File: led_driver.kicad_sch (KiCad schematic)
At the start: 19 parts, among them U1 MP2483DQ-LF-P

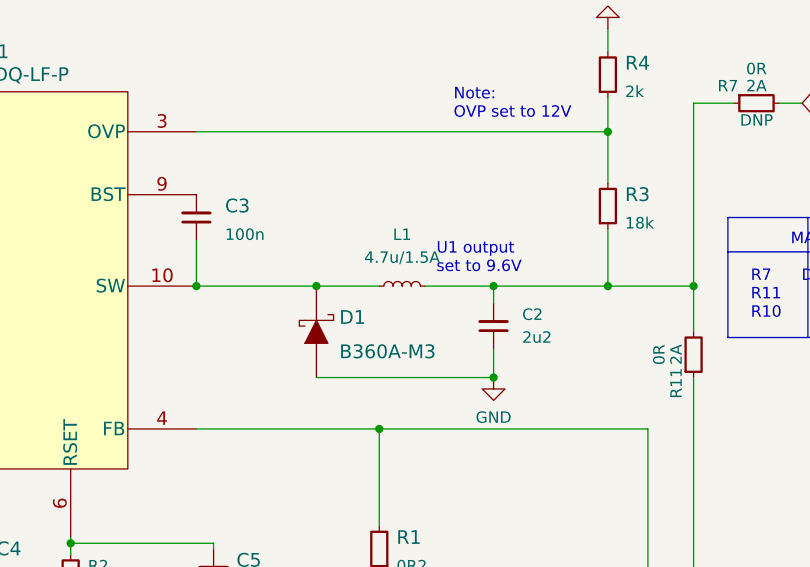
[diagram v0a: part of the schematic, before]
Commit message: Layout tweaks
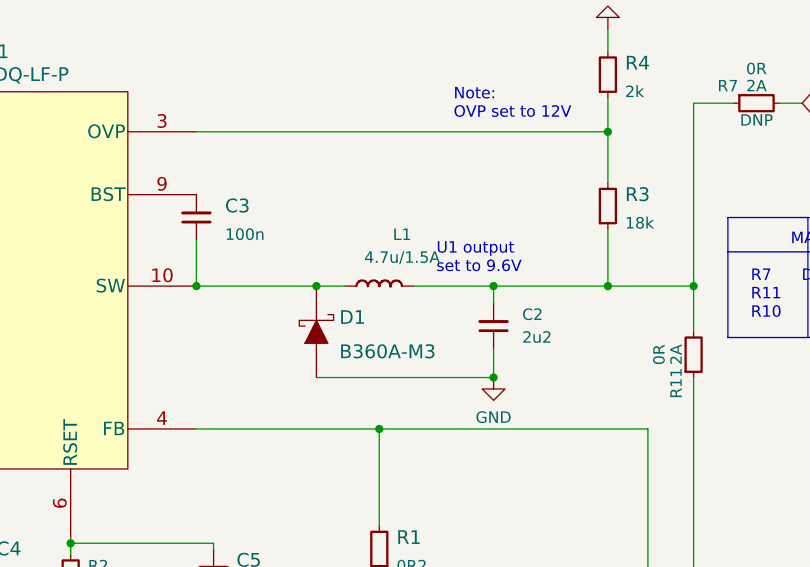
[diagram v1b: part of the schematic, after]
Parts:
- POT1: footprint antmicro-footprints:R0141-2-20k -> antmicro-footprints:Potentiometer_SRPassives_R0141-2_Horizontal
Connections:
- net GND: now also D1.A; no longer D1.1 (A)
- net at C3.1, L1.1 (P), U1.10 (SW): now also D1.K; no longer D1.2 (K)
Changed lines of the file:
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@@
     (stroke (width 0) (type default) (color 0 0 0 0))
   )
-  (wire (pts (xy 168.275 78.105) (xy 175.895 78.105))
+  (wire (pts (xy 167.005 78.105) (xy 175.895 78.105))
     (stroke (width 0) (type default) (color 0 0 0 0))
   )
@@
     (stroke (width 0) (type default) (color 0 0 0 0))
   )
-  (wire (pts (xy 156.21 78.105) (xy 163.195 78.105))
+  (wire (pts (xy 156.21 78.105) (xy 159.385 78.105))
     (stroke (width 0) (type default) (color 0 0 0 0))
   )
@@
       (effects (font (size 1.524 1.524)) (justify left) hide)
     )
-    (pin "1")
-    (pin "2")
+    (pin "A")
+    (pin "K")
   )
   (symbol (lib_id "antmicroResistors0402:R_20k_0402") (at 80.01 95.885 90) (unit 1)
@@
       (effects (font (size 1.27 1.27)) (justify left))
     )
-    (property "Footprint" "antmicro-footprints:R0141-2-20k" (id 2) (at 87.63 54.61 0)
-      (effects (font (size 1.27 1.27)) hide)
-    )
+    (property "Footprint" "antmicro-footprints:Potentiometer_SRPassives_R0141-2_Horizontal" (id 2) (at 87.63 54.61 0)
+      (effects (font (size 1.27 1.27)) hide)
+    )

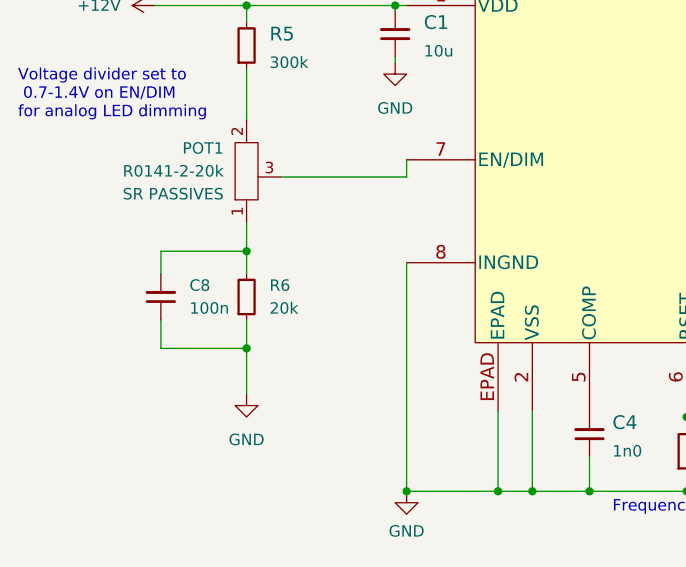
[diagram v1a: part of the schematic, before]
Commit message: Added pull down resistors on USB
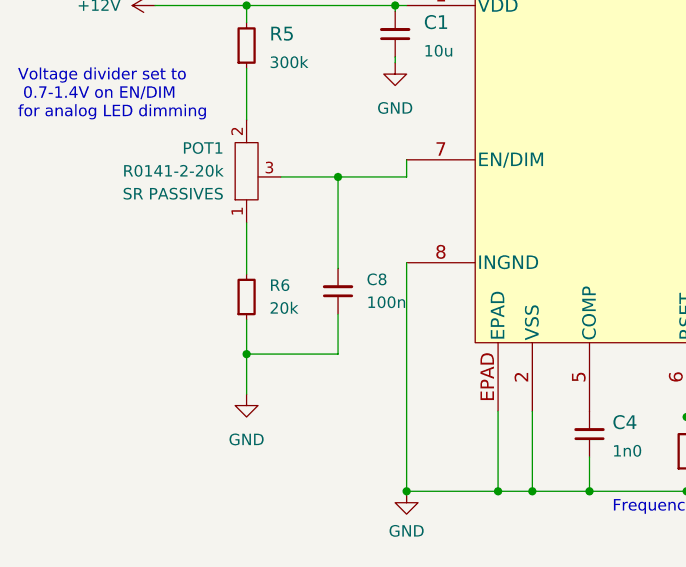
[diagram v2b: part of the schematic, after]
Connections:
- net at POT1.1, R6.2: no longer C8.2
- net at POT1.3, U1.7 (EN/DIM): now also C8.2
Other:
- moved on the sheet: C8
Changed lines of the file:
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@@
   (junction (at 111.76 114.935) (diameter 0) (color 0 0 0 0)
   )
-  (junction (at 80.01 99.06) (diameter 0) (color 0 0 0 0)
-  )
   (junction (at 163.195 93.98) (diameter 0) (color 0 0 0 0)
   )
@@
   (junction (at 97.79 114.935) (diameter 0) (color 0 0 0 0)
   )
-  (junction (at 80.01 88.265) (diameter 0) (color 0 0 0 0)
+  (junction (at 90.17 80.01) (diameter 0) (color 0 0 0 0)
   )
   (junction (at 175.895 78.105) (diameter 0) (color 0 0 0 0)
@@
   (junction (at 96.52 60.96) (diameter 0) (color 0 0 0 0)
   )
+  (junction (at 80.01 99.695) (diameter 0) (color 0 0 0 0)
+  )
   (junction (at 198.12 78.105) (diameter 0) (color 0 0 0 0)
   )
@@
     (stroke (width 0) (type default) (color 0 0 0 0))
   )
-  (wire (pts (xy 70.485 95.885) (xy 70.485 99.06))
-    (stroke (width 0) (type default) (color 0 0 0 0))
-  )
   (wire (pts (xy 111.76 114.935) (xy 111.76 106.045))
     (stroke (width 0) (type default) (color 0 0 0 0))
@@
     (stroke (width 0) (type default) (color 0 0 0 0))
   )
-  (wire (pts (xy 70.485 99.06) (xy 80.01 99.06))
+  (wire (pts (xy 90.17 99.695) (xy 80.01 99.695))
     (stroke (width 0) (type default) (color 0 0 0 0))
   )
@@
     (stroke (width 0) (type default) (color 0 0 0 0))
   )
-  (wire (pts (xy 83.82 80.01) (xy 97.79 80.01))
+  (wire (pts (xy 83.82 80.01) (xy 90.17 80.01))
     (stroke (width 0) (type default) (color 0 0 0 0))
   )
@@
     (stroke (width 0) (type default) (color 0 0 0 0))
   )
+  (wire (pts (xy 90.17 90.17) (xy 90.17 80.01))
+    (stroke (width 0) (type default) (color 0 0 0 0))
+  )
+  (wire (pts (xy 90.17 80.01) (xy 97.79 80.01))
+    (stroke (width 0) (type default) (color 0 0 0 0))
+  )
   (wire (pts (xy 163.195 116.84) (xy 144.78 116.84))
     (stroke (width 0) (type default) (color 0 0 0 0))
@@
     (stroke (width 0) (type default) (color 0 0 0 0))
   )
-  (wire (pts (xy 80.01 88.265) (xy 80.01 90.805))
-    (stroke (width 0) (type default) (color 0 0 0 0))
-  )
   (wire (pts (xy 167.005 78.105) (xy 175.895 78.105))
     (stroke (width 0) (type default) (color 0 0 0 0))
@@
     (stroke (width 0) (type default) (color 0 0 0 0))
   )
-  (wire (pts (xy 80.01 99.06) (xy 80.01 104.14))
-    (stroke (width 0) (type default) (color 0 0 0 0))
-  )
   (wire (pts (xy 188.595 49.53) (xy 188.595 52.07))
     (stroke (width 0) (type default) (color 0 0 0 0))
@@
     (stroke (width 0) (type default) (color 0 0 0 0))
   )
+  (wire (pts (xy 90.17 95.25) (xy 90.17 99.695))
+    (stroke (width 0) (type default) (color 0 0 0 0))
+  )
   (wire (pts (xy 107.95 114.935) (xy 111.76 114.935))
     (stroke (width 0) (type default) (color 0 0 0 0))
   )
-  (wire (pts (xy 70.485 88.265) (xy 80.01 88.265))
-    (stroke (width 0) (type default) (color 0 0 0 0))
-  )
   (wire (pts (xy 156.21 78.105) (xy 159.385 78.105))
     (stroke (width 0) (type default) (color 0 0 0 0))
@@
     (stroke (width 0) (type default) (color 0 0 0 0))
   )
-  (wire (pts (xy 80.01 95.885) (xy 80.01 99.06))
+  (wire (pts (xy 80.01 95.885) (xy 80.01 99.695))
     (stroke (width 0) (type default) (color 0 0 0 0))
   )
@@
     (stroke (width 0) (type default) (color 0 0 0 0))
   )
-  (wire (pts (xy 70.485 90.805) (xy 70.485 88.265))
-    (stroke (width 0) (type default) (color 0 0 0 0))
-  )
   (wire (pts (xy 198.12 88.265) (xy 198.12 123.19))
     (stroke (width 0) (type default) (color 0 0 0 0))
@@
     (stroke (width 0) (type default) (color 0 0 0 0))
   )
+  (wire (pts (xy 80.01 99.695) (xy 80.01 104.14))
+    (stroke (width 0) (type default) (color 0 0 0 0))
+  )
   (wire (pts (xy 118.11 114.935) (xy 111.76 114.935))
     (stroke (width 0) (type default) (color 0 0 0 0))
@@
     (stroke (width 0) (type default) (color 0 0 0 0))
   )
-  (wire (pts (xy 80.01 85.09) (xy 80.01 88.265))
+  (wire (pts (xy 80.01 85.09) (xy 80.01 90.805))
     (stroke (width 0) (type default) (color 0 0 0 0))
   )
@@
     (pin "2")
   )
-  (symbol (lib_id "antmicroCapacitors0402:C_100n_0402") (at 70.485 95.885 90) (unit 1)
+  (symbol (lib_id "antmicroCapacitors0402:C_100n_0402") (at 90.17 95.25 90) (unit 1)
     (in_bom yes) (on_board yes) (fields_autoplaced)
-    (property "Reference" "C8" (id 0) (at 73.66 92.0685 90)
+    (property "Reference" "C8" (id 0) (at 93.345 91.4335 90)
       (effects (font (size 1.27 1.27) (thickness 0.15)) (justify right))
     )
-    (property "Value" "C_100n_0402" (id 1) (at 80.645 75.565 0)
-      (effects (font (size 1.27 1.27) (thickness 0.15)) (justify left bottom) hide)
-    )
-    (property "Footprint" "antmicro-footprints:C_0402_1005Metric" (id 2) (at 83.185 75.565 0)
-      (effects (font (size 1.27 1.27) (thickness 0.15)) (justify left bottom) hide)
-    )
-    (property "Datasheet" "https://search.murata.co.jp/Ceramy/image/img/A01X/G101/ENG/GRM155R61H104KE14-01.pdf" (id 3) (at 85.725 75.565 0)
-      (effects (font (size 1.27 1.27) (thickness 0.15)) (justify left bottom) hide)
-    )
-    (property "MPN" "GRM155R61H104KE14D" (id 4) (at 88.265 75.565 0)
-      (effects (font (size 1.27 1.27) (thickness 0.15)) (justify left bottom) hide)
-    )
-    (property "Manufacturer" "Murata" (id 5) (at 90.805 75.565 0)
-      (effects (font (size 1.27 1.27) (thickness 0.15)) (justify left bottom) hide)
-    )
-    (property "License" "Apache-2.0 License" (id 6) (at 93.345 75.565 0)
-      (effects (font (size 1.27 1.27) (thickness 0.15)) (justify left bottom) hide)
-    )
-    (property "Copyright" "Copyright (c) 2023 Antmicro" (id 7) (at 95.885 75.565 0)
-      (effects (font (size 1.27 1.27) (thickness 0.15)) (justify left bottom) hide)
-    )
-    (property "Val" "100n" (id 8) (at 73.66 94.6085 90)
+    (property "Value" "C_100n_0402" (id 1) (at 100.33 74.93 0)
+      (effects (font (size 1.27 1.27) (thickness 0.15)) (justify left bottom) hide)
+    )
+    (property "Footprint" "antmicro-footprints:C_0402_1005Metric" (id 2) (at 102.87 74.93 0)
+      (effects (font (size 1.27 1.27) (thickness 0.15)) (justify left bottom) hide)
+    )
+    (property "Datasheet" "https://search.murata.co.jp/Ceramy/image/img/A01X/G101/ENG/GRM155R61H104KE14-01.pdf" (id 3) (at 105.41 74.93 0)
+      (effects (font (size 1.27 1.27) (thickness 0.15)) (justify left bottom) hide)
+    )
+    (property "MPN" "GRM155R61H104KE14D" (id 4) (at 107.95 74.93 0)
+      (effects (font (size 1.27 1.27) (thickness 0.15)) (justify left bottom) hide)
+    )
+    (property "Manufacturer" "Murata" (id 5) (at 110.49 74.93 0)
+      (effects (font (size 1.27 1.27) (thickness 0.15)) (justify left bottom) hide)
+    )
+    (property "License" "Apache-2.0 License" (id 6) (at 113.03 74.93 0)
+      (effects (font (size 1.27 1.27) (thickness 0.15)) (justify left bottom) hide)
+    )
+    (property "Copyright" "Copyright (c) 2023 Antmicro" (id 7) (at 115.57 74.93 0)
+      (effects (font (size 1.27 1.27) (thickness 0.15)) (justify left bottom) hide)
+    )
+    (property "Val" "100n" (id 8) (at 93.345 93.9735 90)
       (effects (font (size 1.27 1.27) (thickness 0.15)) (justify right))
     )
-    (property "Voltage" "50V" (id 9) (at 98.425 75.565 0)
-      (effects (font (size 1.27 1.27)) (justify left bottom) hide)
-    )
-    (property "Dielectric" "X5R" (id 10) (at 100.965 75.565 0)
-      (effects (font (size 1.27 1.27)) (justify left bottom) hide)
-    )
+    (property "Voltage" "50V" (id 9) (at 118.11 74.93 0)
+      (effects (font (size 1.27 1.27)) (justify left bottom) hide)
+    )
+    (property "Dielectric" "X5R" (id 10) (at 120.65 74.93 0)
+      (effects (font (size 1.27 1.27)) (justify left bottom) hide)
+    )

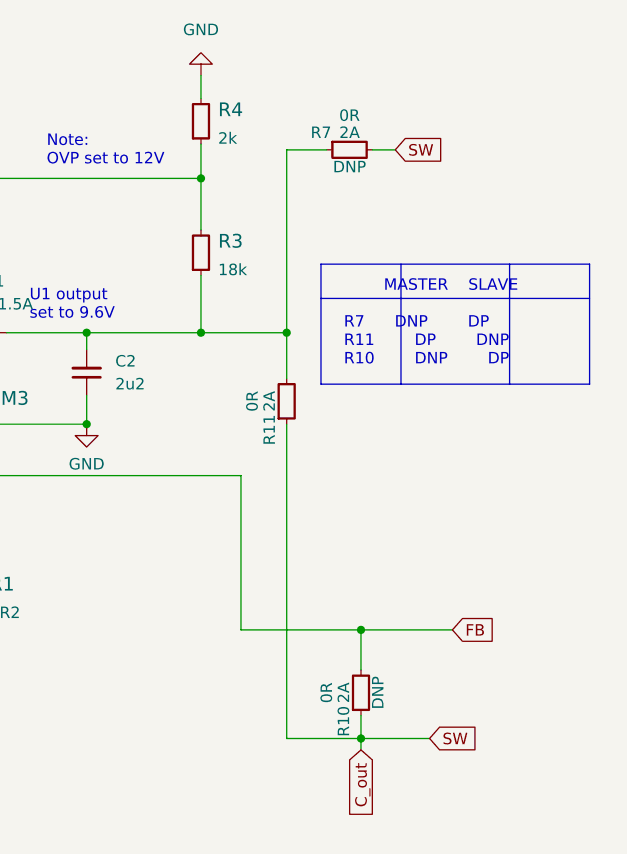
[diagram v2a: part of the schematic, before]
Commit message: Change diodes power rail labels
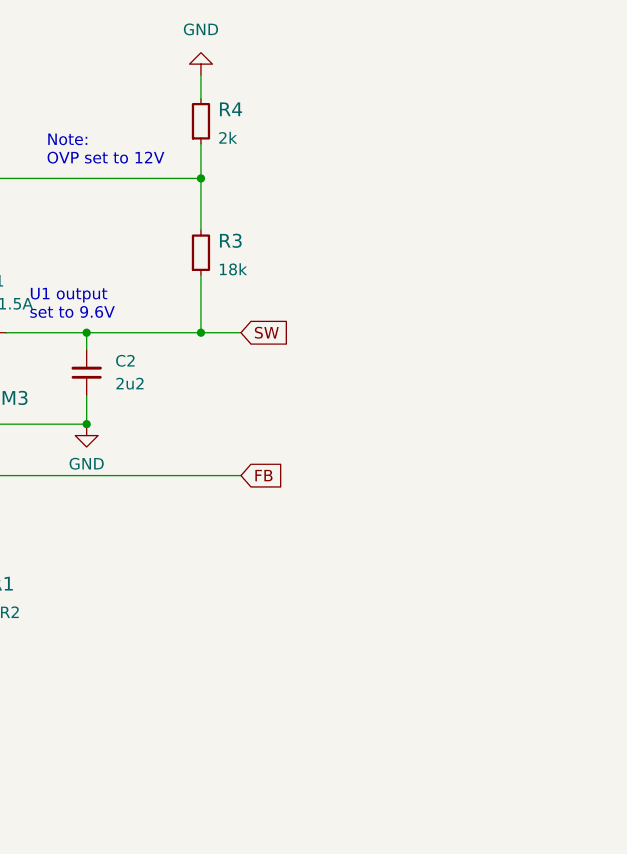
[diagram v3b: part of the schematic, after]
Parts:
- removed R10, R11, R7: R_0R_1206, antmicro-footprints:R_1206_3216Metric, symbol antmicroResistorsmisc:R_0R_1206
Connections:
- net SW: now reaches C2.2, L1.2 (P), R3.1
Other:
- note removed: "MASTER SLAVE R7 DNP DP R11 DP DNP R10 DNP DP"

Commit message: Add 100n to VBUS, schematic cleanup
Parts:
- added C10, C11: C_22u_0603, antmicro-footprints:C_0603_1608Metric, symbol antmicroCapacitors0603:C_22u_0603
- added C12, C7, C9: C_100n_0402, antmicro-footprints:C_0402_1005Metric, symbol antmicroCapacitors0402:C_100n_0402
- added C6: C_10p_0402, antmicro-footprints:C_0402_1005Metric, symbol antmicroCapacitors0402:C_10p_0402
- added J1: BarrelJack_3167288, antmicro-footprints:BarrelJack_3167288_Horizontal, symbol antmicroBarrelAudioConnectors:BarrelJack_3167288
- added J2: USB4105-GF-A, antmicro-footprints:GCT_USB4105-GF-A, symbol antmicroUSBDVIHDMIConnectors:USB4105-GF-A
- added L2: TFM252012ALMA3R3MTAA, antmicro-footprints:L_1008_2520Metric, symbol antmicroFixedInductors:TFM252012ALMA3R3MTAA
- added R12, R14: R_10k_0402, antmicro-footprints:R_0402_1005Metric, symbol antmicroResistors0402:R_10k_0402
- added R13: R_100R_0402, antmicro-footprints:R_0402_1005Metric, symbol antmicroResistors0402:R_100R_0402
- added R8: R_6k8_0402, antmicro-footprints:0402-res, symbol antmicroResistors0402:R_6k8_0402
- added R9: R_1k3_0402, antmicro-footprints:R_0402_1005Metric, symbol antmicroResistors0402:R_1k3_0402
- added TP1: TP_1mm_SMD, antmicro-footprints:TP_SMD_1_MM, symbol antmicroTestPoints:TP_1mm_SMD
- added U2: AP62301Z6-7, antmicro-footprints:SOT-563, symbol antmicroDCDCConverters:AP62301Z6-7
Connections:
- net +12V: now also C6.1, C9.2, J1.1, U2.1 (VIN)
- net GND: now also C10.1, C11.1, C12.1, C6.2, C9.1, J1.2, J1.3, J2.A1 (GND), J2.A12 (GND), J2.B1 (GND), J2.B12 (GND), J2.S1 (SHIELD), R12.1, R14.1, R9.1, U2.3 (GND)
- new net: J2.A6 (D+), J2.B6 (D+), R13.1, R14.2
- new net: J2.A7 (D-), J2.B7 (D-), R12.2, R13.2
- new net: C7.1, U2.4 (BST)
- new net: C7.2, L2.1, U2.2 (SW)
- new net: TP1.1, U2.5 (EN)
- new net: R8.1, R9.2, U2.6 (FB)
- new net VBUS: C10.2, C11.2, C12.2, J2.A4 (VBUS), J2.A9 (VBUS), J2.B4 (VBUS), J2.B9 (VBUS), L2.2, R8.2
- no-connect marks 0 -> 4
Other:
- note added: "12V to 5V Switching regulator"
- note added: "LED Driver"
- note added: "Place close to USB-C VBUS pin"
- note added: "Power input connector"
- note added: "Power supply for the microscope"
- note added: "USB C output"
- note added: "VFB = 0.8025V"
- note added: "VIN: 12V-18V"
- moved on the sheet: C1, C2, C3, C4, C5, C8, D1, L1, POT1, R1, R2, R3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
